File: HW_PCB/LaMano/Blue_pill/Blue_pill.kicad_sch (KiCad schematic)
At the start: 30 parts, among them J1 V_Battery, J2 STLINK, J3 H1, J4 H2, J5 MPU6050, J6 NRF24, SW1 SW_DPST_x2, SW2 SW_DPST_x2, U1 STM32F103C8Tx, U2 AMS1117-3.3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

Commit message: HAND FULL
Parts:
- SW1: footprint Button_Switch_THT:SW_Push_2P1T_Toggle_CK_PVA1xxH4xxxxxxV2 -> SWESPECIAL:SWESPECIAL
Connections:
- net VIN: now also C7.1, U2.3 (VI)
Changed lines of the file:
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@@
 		(color 0 0 0 0)
 	)
-	(junction
-		(at 184.15 63.5)
-		(diameter 0)
-		(color 0 0 0 0)
-	)
 	(wire
 		(pts
@@
 	(wire
 		(pts
-			(xy 180.34 63.5) (xy 184.15 63.5)
+			(xy 180.34 63.5) (xy 185.42 63.5)
 		)
 		(stroke
@@
 	(wire
 		(pts
+			(xy 159.512 143.256) (xy 156.972 143.256)
+		)
+		(stroke
+			(width 0)
+			(type default)
+		)
+	)
+	(wire
+		(pts
 			(xy 71.12 111.76) (xy 77.47 111.76)
 		)
@@
 	(wire
 		(pts
+			(xy 156.972 138.43) (xy 151.13 138.43)
+		)
+		(stroke
+			(width 0)
+			(type default)
+		)
+	)
+	(wire
+		(pts
 			(xy 238.76 88.9) (xy 234.95 88.9)
 		)
@@
 	(wire
 		(pts
-			(xy 184.15 63.5) (xy 185.42 63.5)
-		)
-		(stroke
-			(width 0)
-			(type default)
-		)
-	)
-	(wire
-		(pts
 			(xy 44.45 45.72) (xy 31.75 45.72)
 		)
@@
 	(wire
 		(pts
+			(xy 156.972 143.256) (xy 156.972 138.43)
+		)
+		(stroke
+			(width 0)
+			(type default)
+		)
+	)
+	(wire
+		(pts
 			(xy 137.16 53.34) (xy 140.97 53.34)
 		)
@@
 		)
 	)
+	(global_label "VIN"
+		(shape input)
+		(at 180.34 63.5 180)
+		(fields_autoplaced yes)
+		(effects
+			(font
+				(size 1.27 1.27)
+			)
+			(justify right)
+		)
+		(property "Intersheetrefs" "${INTERSHEET_REFS}"
+			(at 174.3309 63.5 0)
+			(effects
+				(font
+					(size 1.27 1.27)
+				)
+				(justify right)
+				(hide yes)
+			)
+		)
+	)
 	(global_label "GND"
 		(shape input)
@@
 	)
 	(symbol
-		(lib_id "power:PWR_FLAG")
-		(at 184.15 63.5 0)
-		(unit 1)
-		(exclude_from_sim no)
-		(in_bom yes)
-		(on_board yes)
-		(dnp no)
-		(fields_autoplaced yes)
-		(property "Reference" "#FLG02"
-			(at 184.15 61.595 0)
-			(effects
-				(font
-					(size 1.27 1.27)
-				)
-				(hide yes)
-			)
-		)
-		(property "Value" "PWR_FLAG"
-			(at 186.69 62.2299 0)
-			(effects
-				(font
-					(size 1.27 1.27)
-				)
-				(justify left)
-			)
-		)
-		(property "Footprint" ""
-			(at 184.15 63.5 0)
-			(effects
-				(font
-					(size 1.27 1.27)
-				)
-				(hide yes)
-			)
-		)
-		(property "Datasheet" "~"
-			(at 184.15 63.5 0)
-			(effects
-				(font
-					(size 1.27 1.27)
-				)
-				(hide yes)
-			)
-		)
-		(property "Description" "Special symbol for telling ERC where power comes from"
-			(at 184.15 63.5 0)
-			(effects
-				(font
-					(size 1.27 1.27)
-				)
-				(hide yes)
-			)
-		)
-		(pin "1"
-		)
-		(instances
-			(project "Esquematico"
-				(path "/45e4e8b9-0ed0-45ac-9243-1204418424c5"
-					(reference "#FLG02")
-					(unit 1)
-				)
-			)
-		)
-	)
-	(symbol
 		(lib_id "Connector:Conn_01x16_Pin")
 		(at 229.87 106.68 0)
@@
 	)
 	(symbol
-		(lib_id "power:PWR_FLAG")
-		(at 151.13 138.43 0)
-		(unit 1)
-		(exclude_from_sim no)
-		(in_bom yes)
-		(on_board yes)
-		(dnp no)
-		(fields_autoplaced yes)
-		(property "Reference" "#FLG01"
-			(at 151.13 136.525 0)
-			(effects
-				(font
-					(size 1.27 1.27)
-				)
-				(hide yes)
-			)
-		)
-		(property "Value" "PWR_FLAG"
-			(at 153.67 137.1599 0)
-			(effects
-				(font
-					(size 1.27 1.27)
-				)
-				(justify left)
-			)
-		)
-		(property "Footprint" ""
-			(at 151.13 138.43 0)
-			(effects
-				(font
-					(size 1.27 1.27)
-				)
-				(hide yes)
-			)
-		)
-		(property "Datasheet" "~"
-			(at 151.13 138.43 0)
-			(effects
-				(font
-					(size 1.27 1.27)
-				)
-				(hide yes)
-			)
-		)
-		(property "Description" "Special symbol for telling ERC where power comes from"
-			(at 151.13 138.43 0)
-			(effects
-				(font
-					(size 1.27 1.27)
-				)
-				(hide yes)
-			)
-		)
-		(pin "1"
-		)
-		(instances
-			(project "Esquematico"
-				(path "/45e4e8b9-0ed0-45ac-9243-1204418424c5"
-					(reference "#FLG01")
-					(unit 1)
-				)
-			)
-		)
-	)
-	(symbol
 		(lib_id "Device:C")
 		(at 62.23 111.76 270)
@@
 			)
 		)
-		(property "Footprint" "Button_Switch_THT:SW_Push_2P1T_Toggle_CK_PVA1xxH4xxxxxxV2"
+		(property "Footprint" "SWESPECIAL:SWESPECIAL"
 			(at 44.45 55.88 0)
 			(effects

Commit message: Modified Placa Mano
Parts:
- J5: footprint Connector_PinHeader_1.00mm:PinHeader_1x08_P1.00mm_Vertical -> Connector_PinHeader_2.54mm:PinHeader_1x08_P2.54mm_Vertical
- J6: footprint Connector_PinHeader_2.00mm:PinHeader_2x04_P2.00mm_Vertical -> Connector_PinHeader_2.54mm:PinHeader_1x08_P2.54mm_Vertical
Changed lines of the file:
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@@
 			)
 		)
-		(property "Footprint" "Connector_PinHeader_1.00mm:PinHeader_1x08_P1.00mm_Vertical"
+		(property "Footprint" "Connector_PinHeader_2.54mm:PinHeader_1x08_P2.54mm_Vertical"
 			(at 36.83 148.59 0)
 			(effects
@@
 			)
 		)
-		(property "Footprint" "Connector_PinHeader_2.00mm:PinHeader_2x04_P2.00mm_Vertical"
+		(property "Footprint" "Connector_PinHeader_2.54mm:PinHeader_1x08_P2.54mm_Vertical"
 			(at 83.82 142.24 0)
 			(effects

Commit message: Pending to route voltages, expected to do one side
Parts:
- C1: footprint Capacitor_SMD:C_0805_2012Metric -> Capacitor_SMD:C_0805_2012Metric_Pad1.18x1.45mm_HandSolder
- D1, D2, D3: footprint LED_SMD:LED_0603_1608Metric -> LED_SMD:LED_0805_2012Metric
- J6: footprint Connector_PinHeader_2.54mm:PinHeader_1x08_P2.54mm_Vertical -> Connector_PinHeader_2.54mm:PinHeader_2x04_P2.54mm_Vertical
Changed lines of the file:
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@@
 			)
 		)
-		(property "Footprint" "Capacitor_SMD:C_0805_2012Metric"
+		(property "Footprint" "Capacitor_SMD:C_0805_2012Metric_Pad1.18x1.45mm_HandSolder"
 			(at 151.4348 40.64 0)
 			(effects
@@
 			)
 		)
-		(property "Footprint" "LED_SMD:LED_0603_1608Metric"
+		(property "Footprint" "LED_SMD:LED_0805_2012Metric"
 			(at 185.42 44.45 0)
 			(effects
@@
 			)
 		)
-		(property "Footprint" "LED_SMD:LED_0603_1608Metric"
+		(property "Footprint" "LED_SMD:LED_0805_2012Metric"
 			(at 186.69 34.29 0)
 			(effects
@@
 			)
 		)
-		(property "Footprint" "Connector_PinHeader_2.54mm:PinHeader_1x08_P2.54mm_Vertical"
+		(property "Footprint" "Connector_PinHeader_2.54mm:PinHeader_2x04_P2.54mm_Vertical"
 			(at 83.82 142.24 0)
 			(effects
@@
 			)
 		)
-		(property "Footprint" "LED_SMD:LED_0603_1608Metric"
+		(property "Footprint" "LED_SMD:LED_0805_2012Metric"
 			(at 185.42 52.07 0)
 			(effects

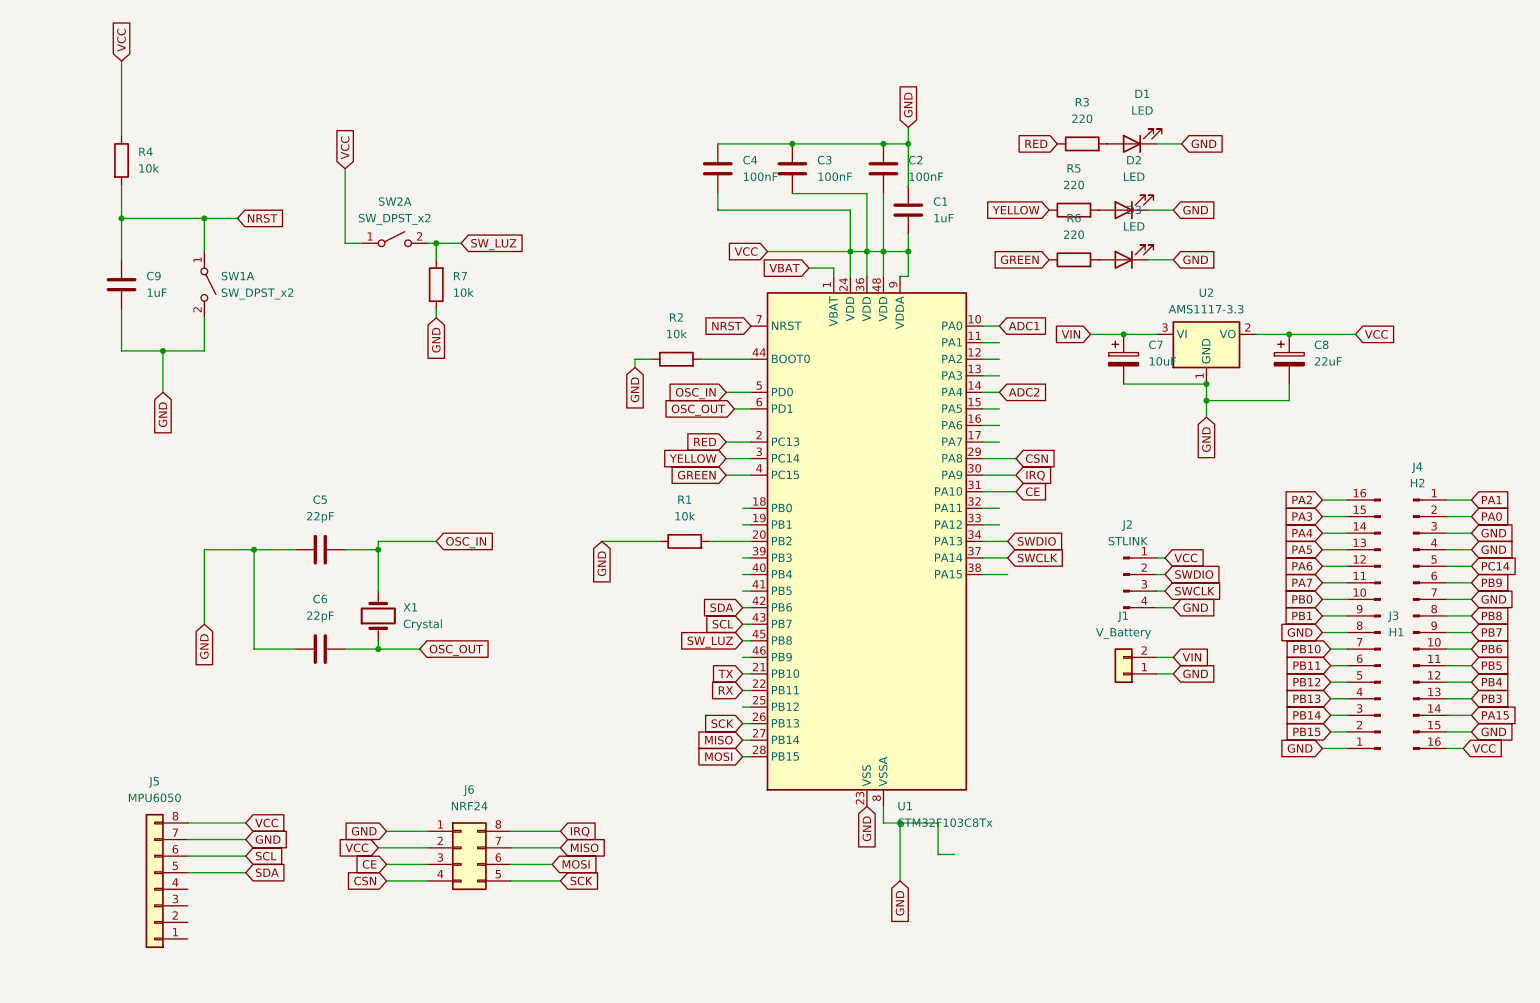
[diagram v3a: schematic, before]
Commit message: 6-29 Added Potentiometer Added Voltage divider for Battery Sensor Changed Layer tracks of NRF24
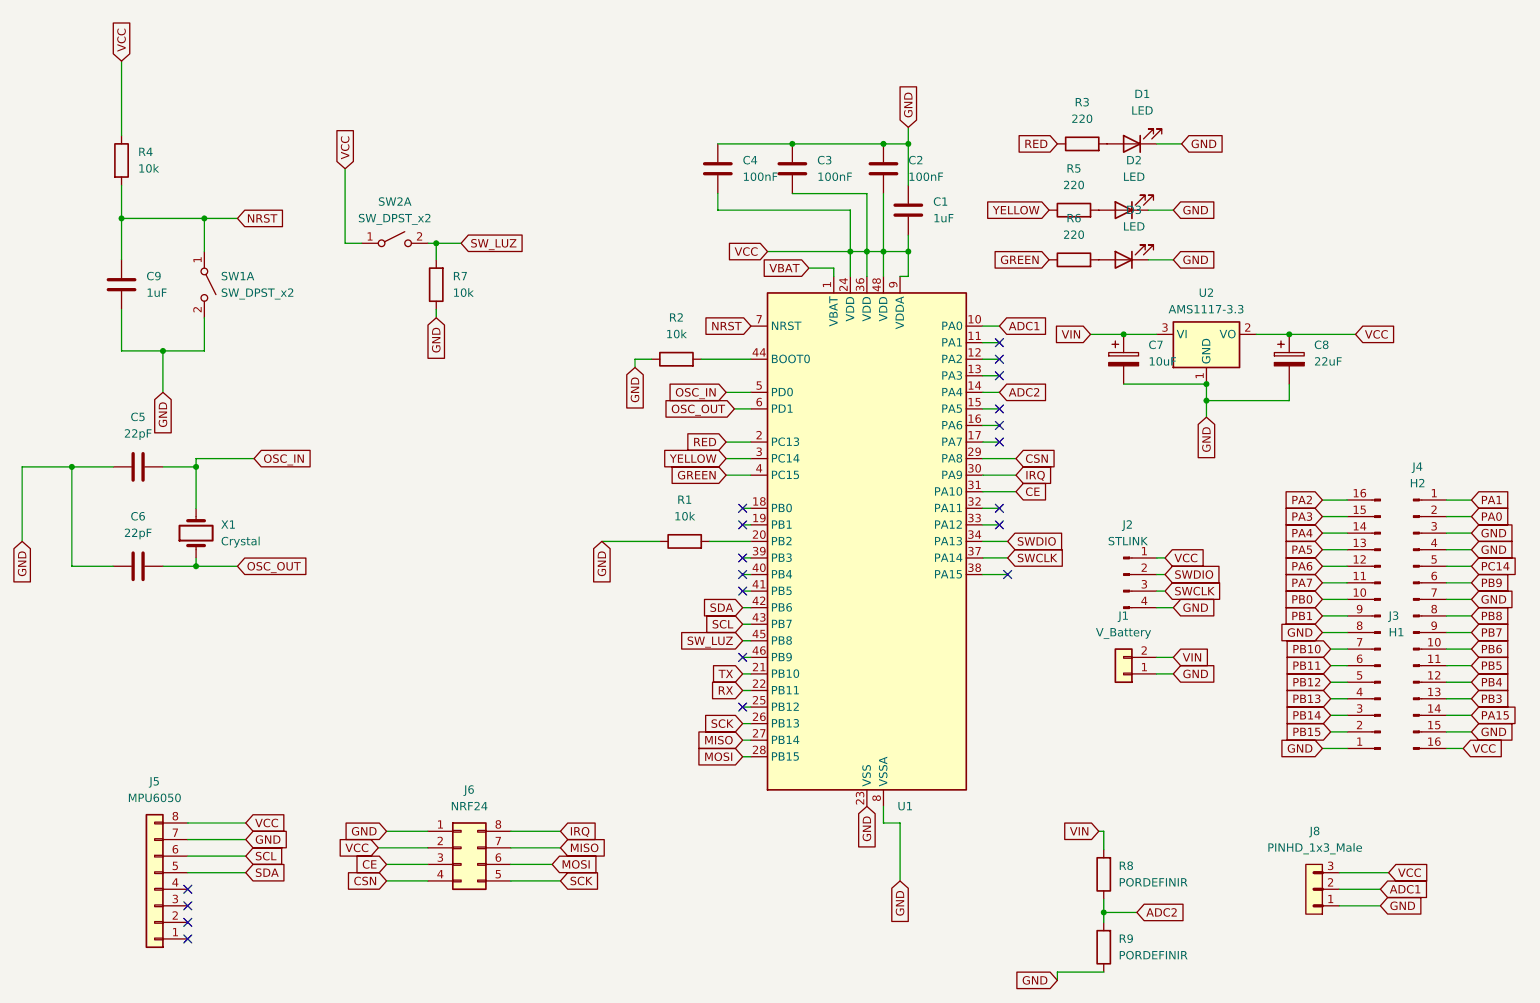
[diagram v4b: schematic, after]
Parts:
- added J8: PINHD_1x3_Male, Connector_PinHeader_2.54mm:PinHeader_1x03_P2.54mm_Vertical, symbol PCM_SL_Pin_Headers:PINHD_1x3_Male
- added R8, R9: PORDEFINIR, Resistor_SMD:R_0805_2012Metric, symbol Device:R
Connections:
- net ADC1: now also J8.2
- net ADC2: now also R8.1, R9.2
- net GND: now also J8.1, R9.1
- net VCC: now also J8.3
- net VIN: now also R8.2
- no-connect marks 0 -> 20
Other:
- moved on the sheet: C5, C6, X1

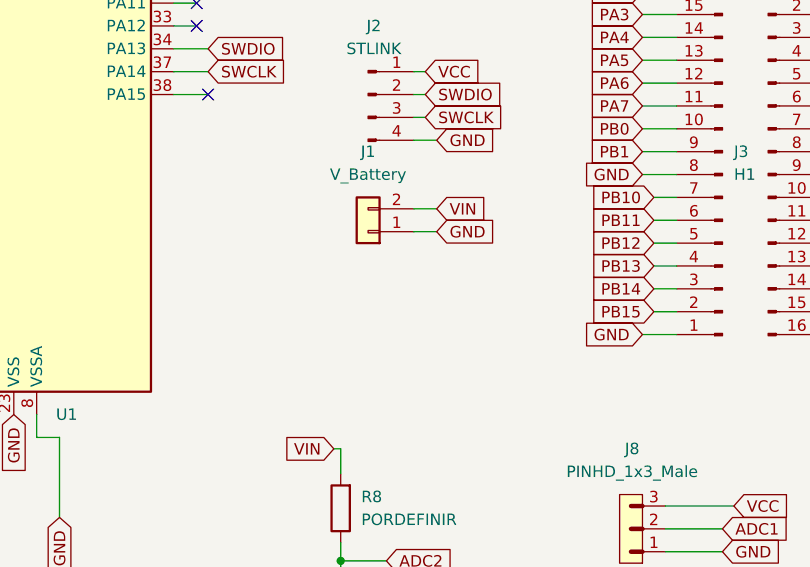
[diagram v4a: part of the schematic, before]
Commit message: 6-29 Fixed MPU orientation Added Vias
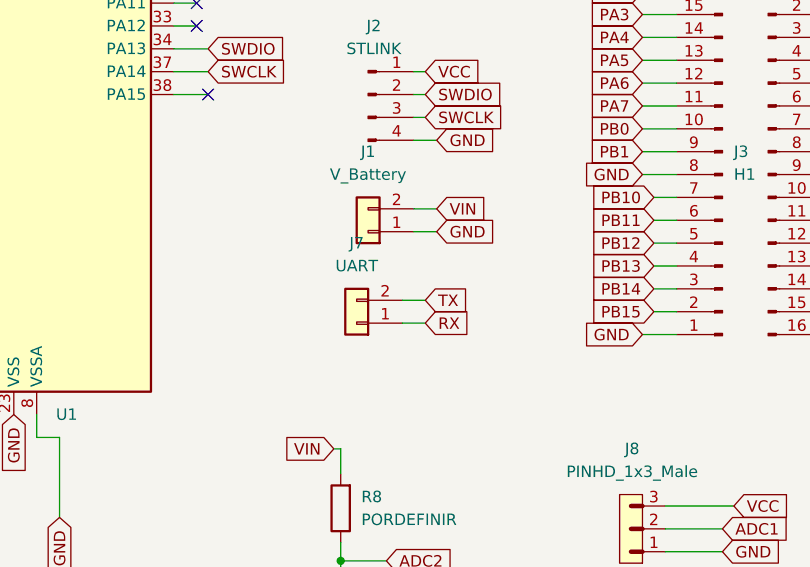
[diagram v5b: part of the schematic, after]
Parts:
- added J7: UART, Connector_PinHeader_2.54mm:PinHeader_1x02_P2.54mm_Vertical, symbol Connector_Generic:Conn_01x02
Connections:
- net RX: now also J7.1 (Pin_1)
- net TX: now also J7.2 (Pin_2)
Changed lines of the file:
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@@
 	(wire
 		(pts
+			(xy 191.77 125.73) (xy 189.23 125.73)
+		)
+		(stroke
+			(width 0)
+			(type default)
+		)
+	)
+	(wire
+		(pts
 			(xy 182.372 152.146) (xy 182.372 153.67)
 		)
@@
 	(wire
 		(pts
+			(xy 191.77 123.19) (xy 189.23 123.19)
+		)
+		(stroke
+			(width 0)
+			(type default)
+		)
+	)
+	(wire
+		(pts
 			(xy 124.46 72.39) (xy 128.27 72.39)
 		)
@@
 		)
 	)
+	(global_label "TX"
+		(shape input)
+		(at 191.77 123.19 0)
+		(fields_autoplaced yes)
+		(effects
+			(font
+				(size 1.27 1.27)
+			)
+			(justify left)
+		)
+		(property "Intersheetrefs" "${INTERSHEET_REFS}"
+			(at 196.9323 123.19 0)
+			(hide yes)
+			(show_name no)
+			(do_not_autoplace no)
+			(effects
+				(font
+					(size 1.27 1.27)
+				)
+				(justify left)
+			)
+		)
+	)
 	(global_label "PB11"
 		(shape input)
@@
 		)
 	)
+	(global_label "RX"
+		(shape input)
+		(at 191.77 125.73 0)
+		(fields_autoplaced yes)
+		(effects
+			(font
+				(size 1.27 1.27)
+			)
+			(justify left)
+		)
+		(property "Intersheetrefs" "${INTERSHEET_REFS}"
+			(at 197.2347 125.73 0)
+			(hide yes)
+			(show_name no)
+			(do_not_autoplace no)
+			(effects
+				(font
+					(size 1.27 1.27)
+				)
+				(justify left)
+			)
+		)
+	)
 	(global_label "PC14"
 		(shape input)
@@
 					(unit 1)
 				)
+			)
+		)
+	)
+	(symbol
+		(lib_id "Connector_Generic:Conn_01x02")
+		(at 184.15 125.73 180)
+		(unit 1)
+		(body_style 1)
+		(exclude_from_sim no)
+		(in_bom yes)
+		(on_board yes)
+		(in_pos_files yes)
+		(dnp no)
+		(fields_autoplaced yes)
+		(property "Reference" "J7"
+			(at 184.15 116.84 0)
+			(show_name no)
+			(do_not_autoplace no)
+			(effects
+				(font
+					(size 1.27 1.27)
+				)
+			)
+		)
+		(property "Value" "UART"
+			(at 184.15 119.38 0)
+			(show_name no)
+			(do_not_autoplace no)
+			(effects
+				(font
+					(size 1.27 1.27)
+				)
+			)
+		)
+		(property "Footprint" "Connector_PinHeader_2.54mm:PinHeader_1x02_P2.54mm_Vertical"
+			(at 184.15 125.73 0)
+			(hide yes)
+			(show_name no)
+			(do_not_autoplace no)
+			(effects
+				(font
+					(size 1.27 1.27)
+				)
+			)
+		)
+		(property "Datasheet" ""
+			(at 184.15 125.73 0)
+			(hide yes)
+			(show_name no)
+			(do_not_autoplace no)
+			(effects
+				(font
+					(size 1.27 1.27)
+				)
+			)
+		)
+		(property "Description" "Generic connector, single row, 01x02, script generated (kicad-library-utils/schlib/autogen/connector/)"
+			(at 184.15 125.73 0)
+			(hide yes)
+			(show_name no)
+			(do_not_autoplace no)
+			(effects
+				(font
+					(size 1.27 1.27)
+				)
+			)
+		)
+		(pin "2"
+		)
+		(pin "1"
+		)
+		(instances
+			(project "Blue_pill"
+				(path "/45e4e8b9-0ed0-45ac-9243-1204418424c5"
+					(reference "J7")
+					(unit 1)
+				)
